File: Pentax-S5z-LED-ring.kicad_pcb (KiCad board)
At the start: 2 copper layers, 40 x 40 mm, 52 parts, among them IC1 ATTINY13-S, P1 CONN_2, P2 +, P3 -, P4 CONN_2, Q1 MOSFET_N, SW1 SW_PUSH, SW2 SW_PUSH

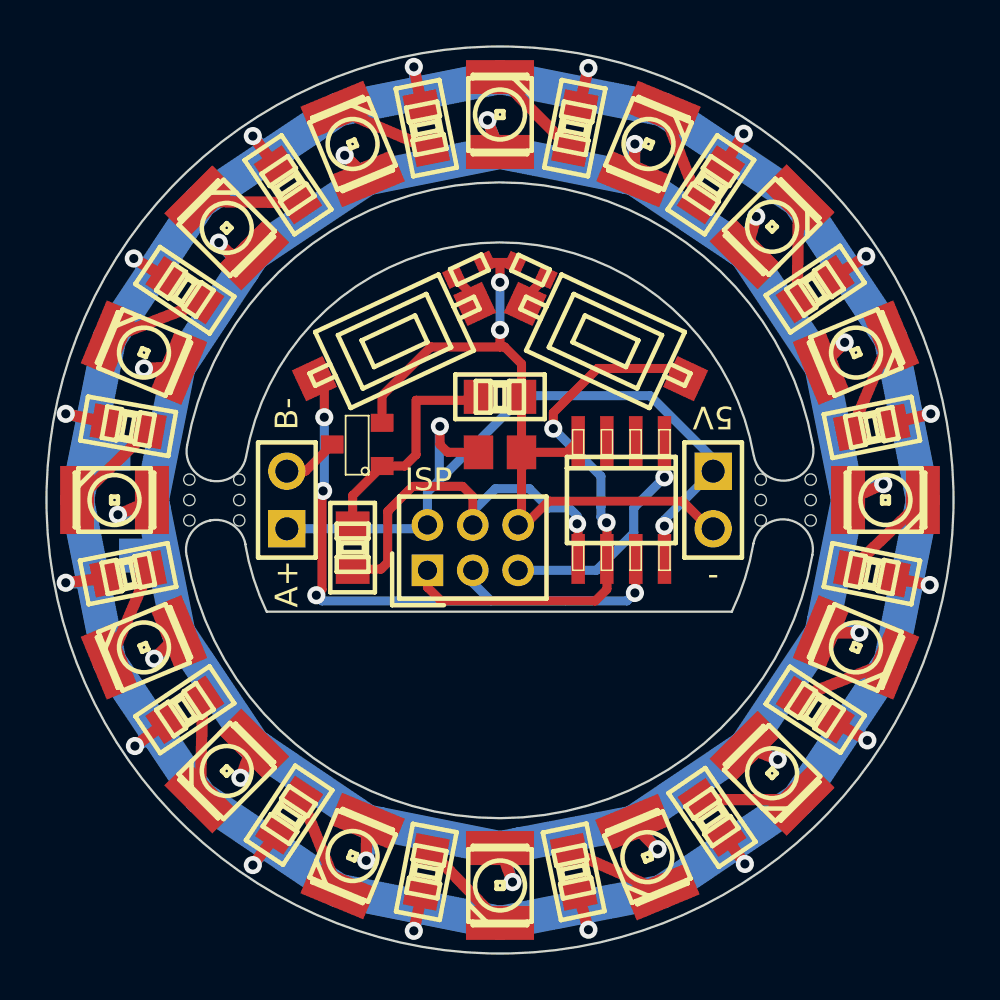
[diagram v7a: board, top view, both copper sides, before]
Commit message: Moved vias away from the outside ring edge.
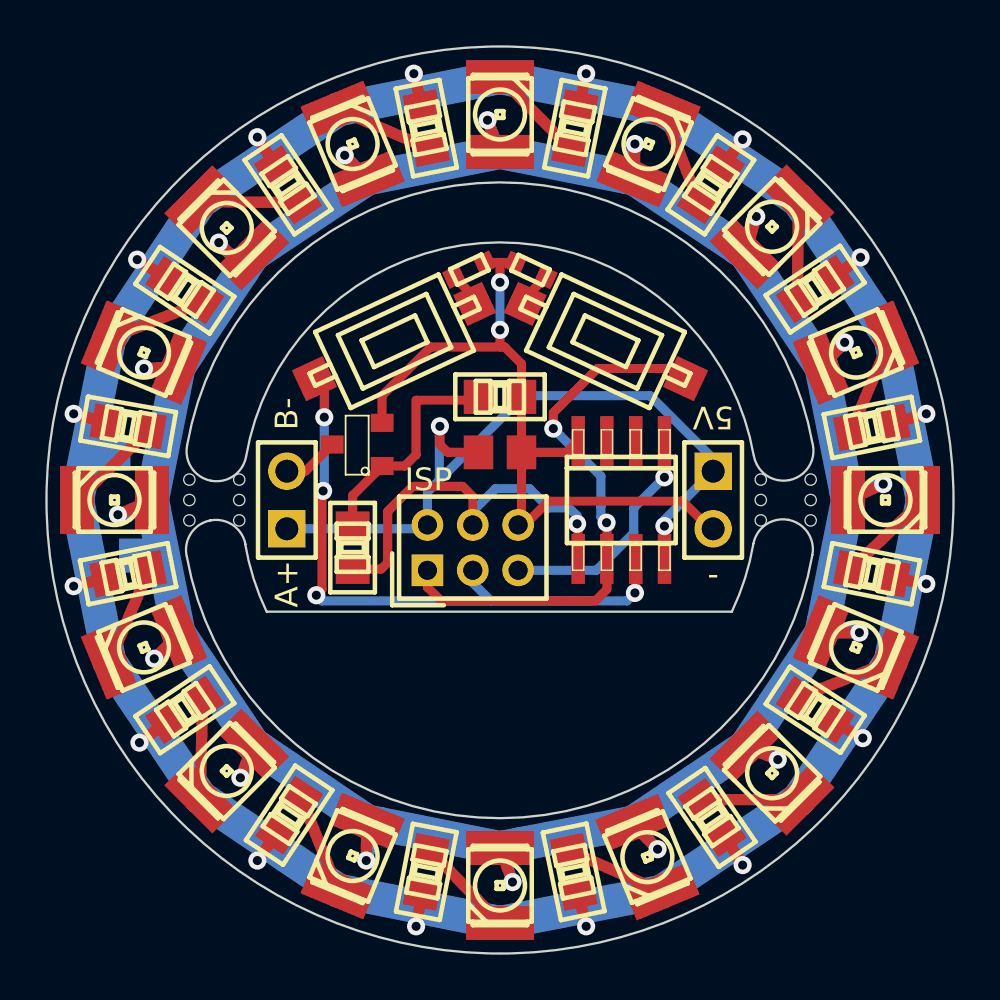
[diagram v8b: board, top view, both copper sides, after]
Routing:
- net N-0000025: track 172.8 -> 165.9 mm
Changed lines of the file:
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@@
-(kicad_pcb (version 3) (host pcbnew "(2013-04-28 BZR 4116)-testing")
+(kicad_pcb (version 3) (host pcbnew "(2013-05-02 BZR 4133)-testing")
   (general
     (links 71)
     (no_connects 0)
-    (area 44.949999 44.949999 85.050001 85.050001)
+    (area 44.422949 44.422949 85.577051 85.577051)
     (thickness 1.6)
     (drawings 26)
@@
   (segment (start 46.366984 65.084961) (end 47.079649 68.650002) (width 0.5) (layer B.Cu) (net 21))
   (segment (start 46.366984 65.084961) (end 47.049676 68.500065) (width 0.5) (layer B.Cu) (net 21))
-  (segment (start 82.917417 61.335321) (end 84 61.2) (width 0.5) (layer B.Cu) (net 21))
-  (via (at 84 61.2) (size 0.8) (layers F.Cu B.Cu) (net 21))
-  (segment (start 84 61.2) (end 82.331545 61.613859) (width 0.5) (layer F.Cu) (net 21))
-  (segment (start 82.942634 68.538533) (end 83.95 68.75) (width 0.5) (layer B.Cu) (net 21))
-  (via (at 83.95 68.75) (size 0.8) (layers F.Cu B.Cu) (net 21))
-  (segment (start 83.95 68.75) (end 82.331545 68.436141) (width 0.5) (layer F.Cu) (net 21))
-  (segment (start 68.771562 82.922495) (end 68.9 83.95) (width 0.5) (layer B.Cu) (net 21))
-  (via (at 68.9 83.95) (size 0.8) (layers F.Cu B.Cu) (net 21))
-  (segment (start 68.9 83.95) (end 68.44264 82.330223) (width 0.5) (layer F.Cu) (net 21))
-  (segment (start 61.331483 47.08335) (end 61.2 45.9) (width 0.5) (layer B.Cu) (net 21))
-  (via (at 61.2 45.9) (size 0.8) (layers F.Cu B.Cu) (net 21))
-  (segment (start 61.2 45.9) (end 61.563859 47.668455) (width 0.5) (layer F.Cu) (net 21))
-  (segment (start 68.597203 47.064088) (end 68.9 45.95) (width 0.5) (layer B.Cu) (net 21))
-  (via (at 68.9 45.95) (size 0.8) (layers F.Cu B.Cu) (net 21))
-  (segment (start 68.9 45.95) (end 68.486141 47.668455) (width 0.5) (layer F.Cu) (net 21))
-  (segment (start 61.514056 82.953147) (end 61.2 84) (width 0.5) (layer B.Cu) (net 21))
-  (via (at 61.2 84) (size 0.8) (layers F.Cu B.Cu) (net 21))
-  (segment (start 61.2 84) (end 61.570367 82.332821) (width 0.5) (layer F.Cu) (net 21))
-  (segment (start 54.763369 80.326069) (end 54.1 81.1) (width 0.5) (layer B.Cu) (net 21))
-  (via (at 54.1 81.1) (size 0.8) (layers F.Cu B.Cu) (net 21))
-  (segment (start 54.1 81.1) (end 55.175682 79.692158) (width 0.5) (layer F.Cu) (net 21))
-  (segment (start 49.952336 75.382295) (end 48.9 75.85) (width 0.5) (layer B.Cu) (net 21))
-  (via (at 48.9 75.85) (size 0.8) (layers F.Cu B.Cu) (net 21))
-  (segment (start 48.9 75.85) (end 50.311522 74.779836) (width 0.5) (layer F.Cu) (net 21))
-  (segment (start 45.85 68.65) (end 47.079649 68.65) (width 0.5) (layer B.Cu) (net 21))
-  (via (at 45.85 68.65) (size 0.8) (layers F.Cu B.Cu) (net 21))
-  (segment (start 47.668455 68.436141) (end 45.85 68.65) (width 0.5) (layer F.Cu) (net 21))
+  (segment (start 82.917417 61.335321) (end 83.8 61.2) (width 0.5) (layer B.Cu) (net 21))
+  (via (at 83.8 61.2) (size 0.8) (layers F.Cu B.Cu) (net 21))
+  (segment (start 83.8 61.2) (end 82.331545 61.613859) (width 0.5) (layer F.Cu) (net 21))
+  (segment (start 82.942634 68.538533) (end 83.8 68.7) (width 0.5) (layer B.Cu) (net 21))
+  (via (at 83.8 68.7) (size 0.8) (layers F.Cu B.Cu) (net 21))
+  (segment (start 83.8 68.7) (end 82.331545 68.436141) (width 0.5) (layer F.Cu) (net 21))
+  (segment (start 68.771562 82.922495) (end 68.8 83.8) (width 0.5) (layer B.Cu) (net 21))
+  (via (at 68.8 83.8) (size 0.8) (layers F.Cu B.Cu) (net 21))
+  (segment (start 68.8 83.8) (end 68.44264 82.330223) (width 0.5) (layer F.Cu) (net 21))
+  (segment (start 61.331483 47.08335) (end 61.2 46.2) (width 0.5) (layer B.Cu) (net 21))
+  (via (at 61.2 46.2) (size 0.8) (layers F.Cu B.Cu) (net 21))
+  (segment (start 61.2 46.2) (end 61.563859 47.668455) (width 0.5) (layer F.Cu) (net 21))
+  (segment (start 68.597203 47.064088) (end 68.8 46.2) (width 0.5) (layer B.Cu) (net 21))
+  (via (at 68.8 46.2) (size 0.8) (layers F.Cu B.Cu) (net 21))
+  (segment (start 68.8 46.2) (end 68.486141 47.668455) (width 0.5) (layer F.Cu) (net 21))
+  (segment (start 61.514056 82.953147) (end 61.3 83.8) (width 0.5) (layer B.Cu) (net 21))
+  (via (at 61.3 83.8) (size 0.8) (layers F.Cu B.Cu) (net 21))
+  (segment (start 61.3 83.8) (end 61.570367 82.332821) (width 0.5) (layer F.Cu) (net 21))
+  (segment (start 54.763369 80.326069) (end 54.3 80.9) (width 0.5) (layer B.Cu) (net 21))
+  (via (at 54.3 80.9) (size 0.8) (layers F.Cu B.Cu) (net 21))
+  (segment (start 54.3 80.9) (end 55.175682 79.692158) (width 0.5) (layer F.Cu) (net 21))
+  (segment (start 49.952336 75.382295) (end 49.1 75.7) (width 0.5) (layer B.Cu) (net 21))
+  (via (at 49.1 75.7) (size 0.8) (layers F.Cu B.Cu) (net 21))
+  (segment (start 49.1 75.7) (end 50.311522 74.779836) (width 0.5) (layer F.Cu) (net 21))
+  (segment (start 46.2 68.8) (end 47.079649 68.65) (width 0.5) (layer B.Cu) (net 21))
+  (via (at 46.2 68.8) (size 0.8) (layers F.Cu B.Cu) (net 21))
+  (segment (start 47.668455 68.436141) (end 46.2 68.8) (width 0.5) (layer F.Cu) (net 21))
   (segment (start 47.079649 68.65) (end 47.079649 68.650002) (width 0.5) (layer B.Cu) (net 21))
-  (segment (start 47.057361 61.461492) (end 45.85 61.2) (width 0.5) (layer B.Cu) (net 21))
-  (via (at 45.85 61.2) (size 0.8) (layers F.Cu B.Cu) (net 21))
-  (segment (start 45.85 61.2) (end 47.664472 61.585041) (width 0.5) (layer F.Cu) (net 21))
+  (segment (start 47.057361 61.461492) (end 46.2 61.2) (width 0.5) (layer B.Cu) (net 21))
+  (via (at 46.2 61.2) (size 0.8) (layers F.Cu B.Cu) (net 21))
+  (segment (start 46.2 61.2) (end 47.664472 61.585041) (width 0.5) (layer F.Cu) (net 21))
   (segment (start 82.917417 61.335323) (end 82.917417 61.335321) (width 0.5) (layer B.Cu) (net 21))
-  (segment (start 50.309677 55.22292) (end 48.85 54.35) (width 0.5) (layer F.Cu) (net 21))
-  (segment (start 49.421588 54.921588) (end 48.85 54.35) (width 0.5) (layer B.Cu) (net 21))
-  (via (at 48.85 54.35) (size 0.8) (layers F.Cu B.Cu) (net 21))
+  (segment (start 50.309677 55.22292) (end 49 54.4) (width 0.5) (layer F.Cu) (net 21))
+  (segment (start 49.421588 54.921588) (end 49 54.4) (width 0.5) (layer B.Cu) (net 21))
+  (via (at 49 54.4) (size 0.8) (layers F.Cu B.Cu) (net 21))
   (segment (start 49.421588 54.921588) (end 49.732512 54.921588) (width 0.5) (layer B.Cu) (net 21))
-  (segment (start 55.120164 50.311522) (end 54.1 48.95) (width 0.5) (layer F.Cu) (net 21))
-  (segment (start 54.775401 49.625401) (end 54.1 48.95) (width 0.5) (layer B.Cu) (net 21))
-  (via (at 54.1 48.95) (size 0.8) (layers F.Cu B.Cu) (net 21))
+  (segment (start 55.120164 50.311522) (end 54.3 49) (width 0.5) (layer F.Cu) (net 21))
+  (segment (start 54.775401 49.625401) (end 54.3 49) (width 0.5) (layer B.Cu) (net 21))
+  (via (at 54.3 49) (size 0.8) (layers F.Cu B.Cu) (net 21))
   (segment (start 54.775401 49.625401) (end 54.775401 49.838125) (width 0.5) (layer B.Cu) (net 21))
-  (segment (start 74.82708 50.309677) (end 75.75 48.85) (width 0.5) (layer F.Cu) (net 21))
-  (segment (start 75.20118 49.39882) (end 75.75 48.85) (width 0.5) (layer B.Cu) (net 21))
-  (via (at 75.75 48.85) (size 0.8) (layers F.Cu B.Cu) (net 21))
+  (segment (start 74.82708 50.309677) (end 75.7 49.1) (width 0.5) (layer F.Cu) (net 21))
+  (segment (start 75.20118 49.39882) (end 75.7 49.1) (width 0.5) (layer B.Cu) (net 21))
+  (via (at 75.7 49.1) (size 0.8) (layers F.Cu B.Cu) (net 21))
   (segment (start 75.20118 49.39882) (end 75.20118 49.797584) (width 0.5) (layer B.Cu) (net 21))
-  (segment (start 79.690323 55.17292) (end 81.15 54.25) (width 0.5) (layer F.Cu) (net 21))
-  (segment (start 80.497672 54.902328) (end 81.15 54.25) (width 0.5) (layer B.Cu) (net 21))
-  (via (at 81.15 54.25) (size 0.8) (layers F.Cu B.Cu) (net 21))
+  (segment (start 79.690323 55.17292) (end 80.9 54.3) (width 0.5) (layer F.Cu) (net 21))
+  (segment (start 80.497672 54.902328) (end 80.9 54.3) (width 0.5) (layer B.Cu) (net 21))
+  (via (at 80.9 54.3) (size 0.8) (layers F.Cu B.Cu) (net 21))
   (segment (start 80.497672 54.902328) (end 80.24651 54.902328) (width 0.5) (layer B.Cu) (net 21))
-  (segment (start 79.695799 74.768775) (end 81.2 75.6) (width 0.5) (layer F.Cu) (net 21))
-  (segment (start 80.651543 75.051543) (end 81.2 75.6) (width 0.5) (layer B.Cu) (net 21))
-  (via (at 81.2 75.6) (size 0.8) (layers F.Cu B.Cu) (net 21))
+  (segment (start 79.695799 74.768775) (end 81 75.5) (width 0.5) (layer F.Cu) (net 21))
+  (segment (start 80.651543 75.051543) (end 81 75.5) (width 0.5) (layer B.Cu) (net 21))
+  (via (at 81 75.5) (size 0.8) (layers F.Cu B.Cu) (net 21))
   (segment (start 80.651543 75.051543) (end 80.277269 75.051543) (width 0.5) (layer B.Cu) (net 21))
-  (segment (start 74.885327 79.78476) (end 75.8 81.05) (width 0.5) (layer F.Cu) (net 21))
-  (segment (start 75.182678 80.432678) (end 75.8 81.05) (width 0.5) (layer B.Cu) (net 21))
-  (via (at 75.8 81.05) (size 0.8) (layers F.Cu B.Cu) (net 21))
+  (segment (start 74.885327 79.78476) (end 75.7 81.1) (width 0.5) (layer F.Cu) (net 21))
+  (segment (start 75.182678 80.432678) (end 75.7 81.1) (width 0.5) (layer B.Cu) (net 21))
+  (via (at 75.7 81.1) (size 0.8) (layers F.Cu B.Cu) (net 21))
   (segment (start 75.182678 80.432678) (end 75.182678 80.222973) (width 0.5) (layer B.Cu) (net 21))
   (segment (start 54.763369 80.436631) (end 54.763369 80.326069) (width 0.5) (layer B.Cu) (net 21))
